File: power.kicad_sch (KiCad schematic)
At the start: 90 parts

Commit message: More work in progres
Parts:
- L41, L42, L43, L44, L45, L46, L47, L48: renamed from L?; value L_Ferrite_Power -> 100
- R402: renamed from R?; value 30k -> 51k
- R403: renamed from R?; value 240k -> 180k
- R432: renamed from R?; value 20k -> 12k
- R433: renamed from R?; value 160k -> 240k
- gave numbers to parts that had none: 76
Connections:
- net +1V8A: now also U42.11 (OUT2), U42.12 (OUT2); no longer U42.14 (OUT1), U42.15 (OUT1)
- net +2V5: now also U42.14 (OUT1), U42.15 (OUT1); no longer U41.14 (OUT1), U41.15 (OUT1)
- net +3V3A: now also U41.11 (OUT2), U41.12 (OUT2); no longer U42.11 (OUT2), U42.12 (OUT2)
- net +5VA: now also U41.14 (OUT1), U41.15 (OUT1); no longer U41.11 (OUT2), U41.12 (OUT2)
- net at C433.2, R431.1, R432.2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: now also U42.10 (FB2); no longer U42.16 (FB1)
- net at C414.2, R411.1, R412.2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: now also U41.10 (FB2); no longer U42.10 (FB2)
- net at U42.4 (IN2), U42.5 (IN2), U42.6 (EN2): now also C431.1, L44.2; no longer C411.1, C412.1, L42.2
- net at U42.7 (NR_SS2): now also C432.1; no longer C413.1
- net at C404.2, R401.1, R402.2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: now also U41.16 (FB1); no longer U41.10 (FB2)
- net at U42.1 (IN1), U42.2 (IN1), U42.20 (EN1): now also C421.1, L43.2; no longer C431.1, L44.2
- net at C401.1, C402.1, L41.2: now also U41.1 (IN1), U41.2 (IN1), U41.20 (EN1); no longer U41.4 (IN2), U41.5 (IN2), U41.6 (EN2)
- net at C403.1: now also U41.19 (NR_SS1); no longer U41.7 (NR_SS2)
- net at C423.2, R421.1, R422.2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: now also U42.16 (FB1); no longer U41.16 (FB1)
- net at C422.1: now also U42.19 (NR_SS1); no longer U41.19 (NR_SS1)
- new net: C411.1, C412.1, L42.2, U41.4 (IN2), U41.5 (IN2), U41.6 (EN2)
- new net: C413.1, U41.7 (NR_SS2)
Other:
- note added: "Margined to 5.1V"
- moved on the sheet: L47, R461, TP462

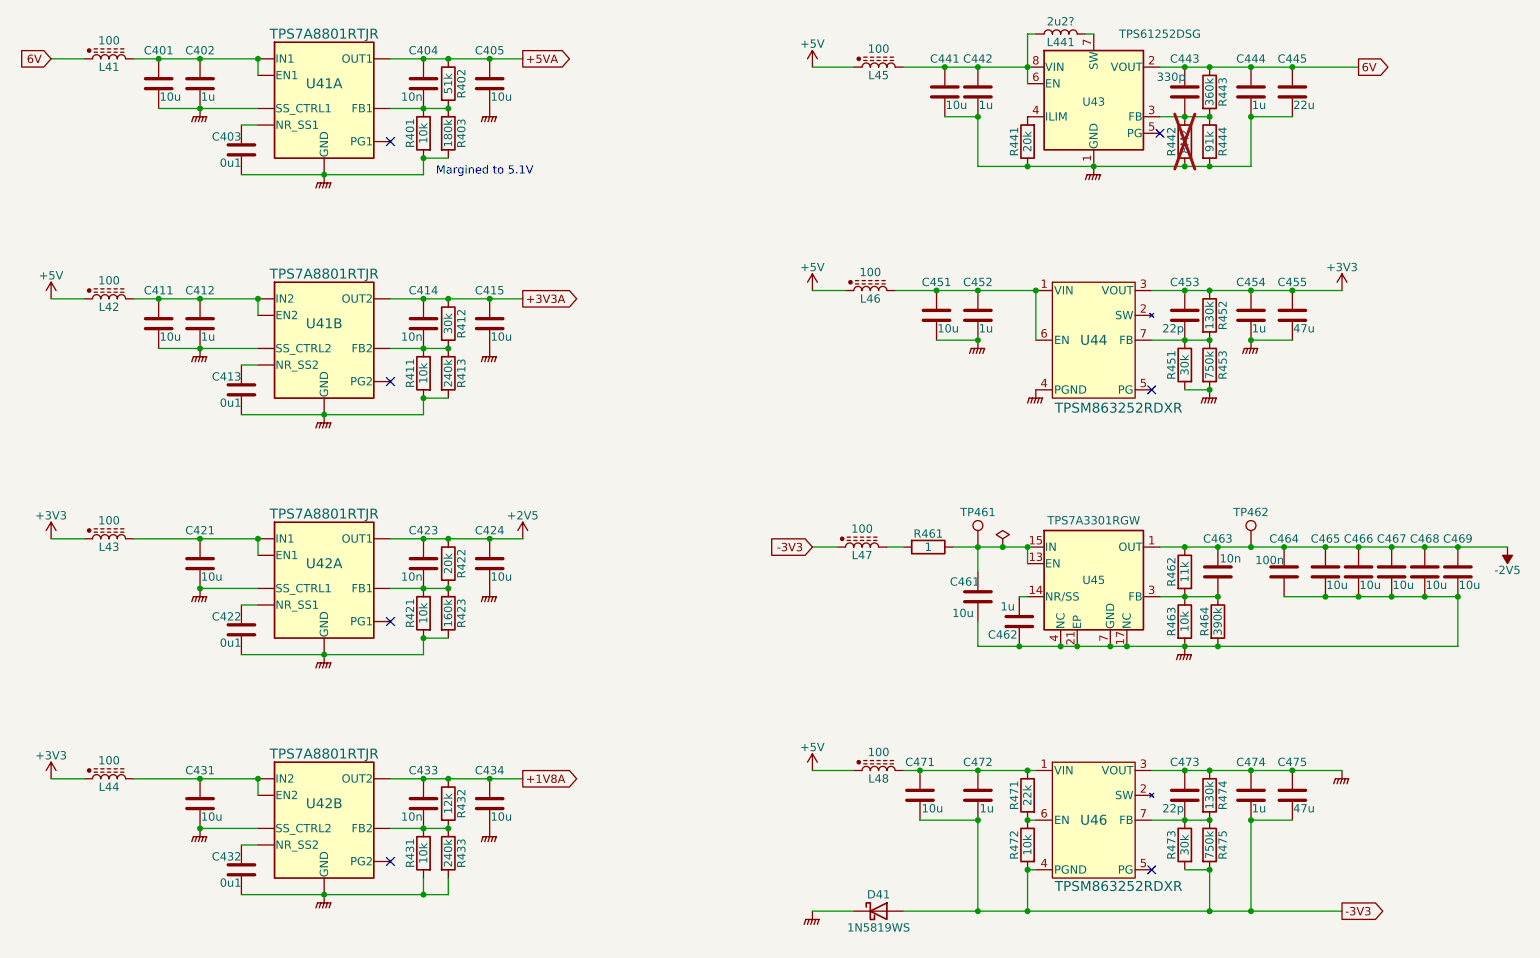
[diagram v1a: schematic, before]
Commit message: Analog side is more or less complete.
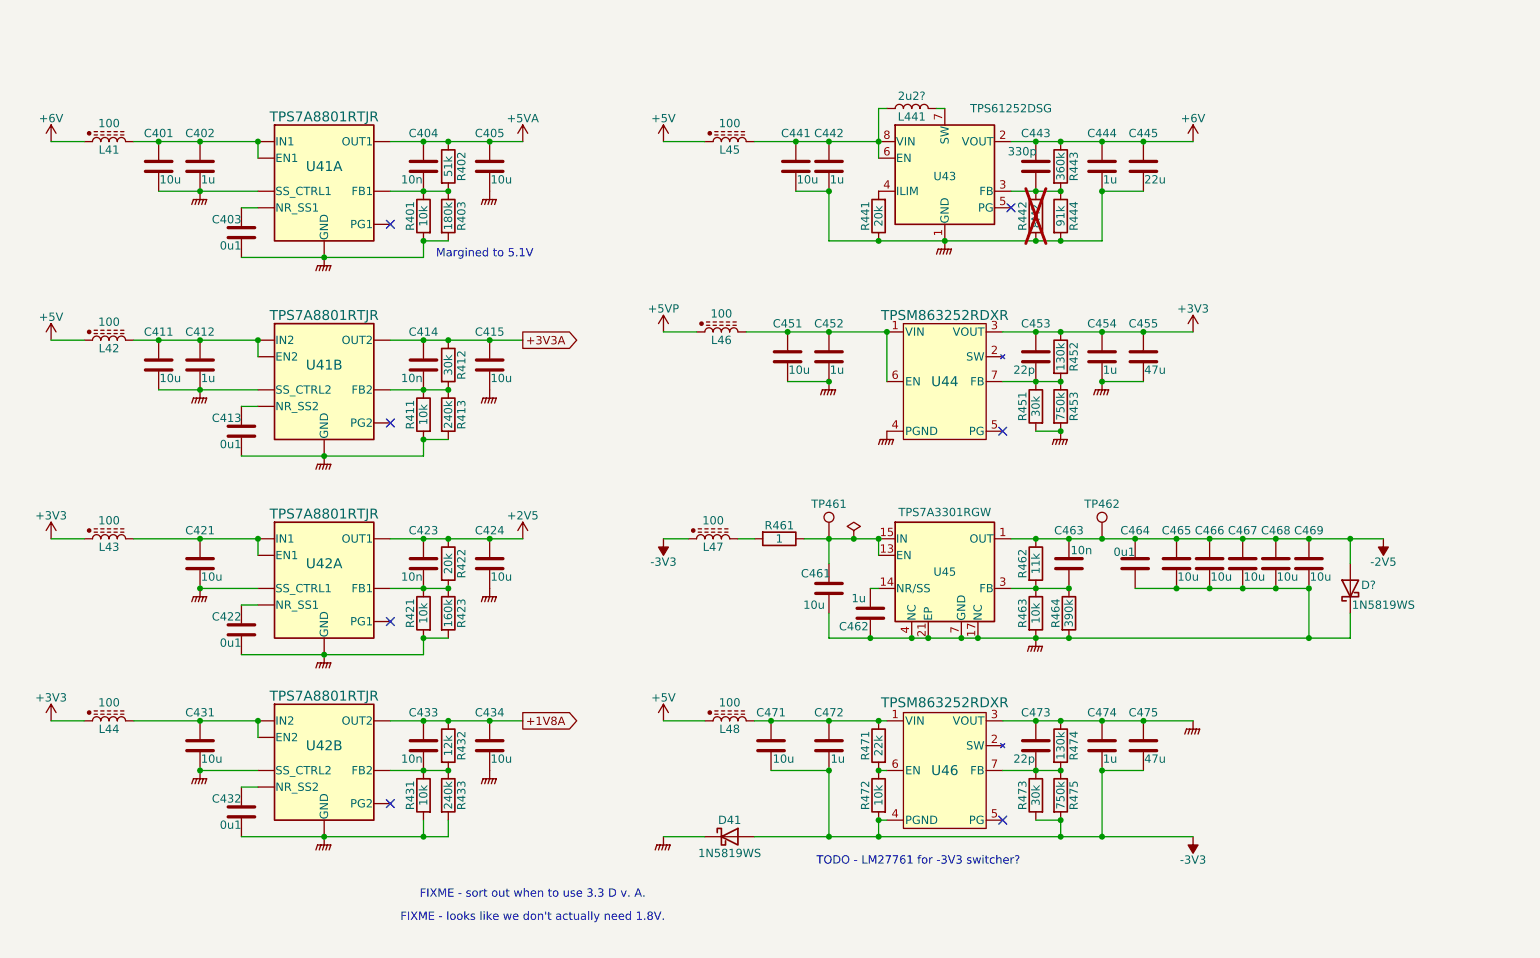
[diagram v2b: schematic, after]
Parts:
- added D?: 1N5819WS, Diode_SMD:D_SOD-323, symbol Diode:1N5819WS
- C464: value 100n -> 0u1
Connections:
- net +5V: no longer L46.1
- net -2V5: now also D?.2 (A)
- net GND: now also D?.1 (K)
- net 6V renamed +6V
- new net +5VP: L46.1
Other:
- note added: "FIXME - looks like we don't actually need 1.8V."
- note added: "FIXME - sort out when to use 3.3 D v. A."
- note added: "TODO - LM27761 for -3V3 switcher?"
- moved on the sheet: C401, C402, C403, C404, C405, C411, C412, C413, C414, C415, C431, C432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

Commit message: Little simplifications etc.
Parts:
- added TP41, TP42, TP43, TP44, TP45, TP46, TP47, TP48: TestPoint, Parts:TestPoint_THTPad_D1.0mm_Drill0.5mm, symbol Connector:TestPoint
- gave numbers to parts that had none: 1
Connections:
- net +1V8A: now also TP47.1
- net +2V5: now also TP45.1
- net +3V3: now also TP43.1
- net +3V3A: now also TP44.1
- net +5VA: now also TP41.1
- net +6V: now also TP42.1
- net -2V5: now also TP46.1
- net -3V3: now also TP48.1

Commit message: Schematic complete, maybe
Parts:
- removed C467, C468, C469: 10u, Capacitor_SMD:C_0402_1005Metric, symbol Device:C
- removed TP461, TP462: TestPoint, Parts:TestPoint_THTPad_D1.0mm_Drill0.5mm, symbol Connector:TestPoint
- added C422, C432: 1u, Capacitor_SMD:C_0402_1005Metric, symbol Device:C
- added C456, C476: 22u, Capacitor_SMD:C_0805_2012Metric, symbol Device:C
- added TP49: TestPoint, Parts:TestPoint_THTPad_D1.0mm_Drill0.5mm, symbol Connector:TestPoint
- C404, C414, C423, C433: footprint (none) -> Capacitor_SMD:C_0603_1608Metric; LCSC (none) -> C307500
- C405, C415, C424, C434: footprint Capacitor_SMD:C_0402_1005Metric -> Capacitor_SMD:C_0603_1608Metric; LCSC C15525 -> C96446
- C443: footprint Capacitor_SMD:C_0402_1005Metric -> Capacitor_SMD:C_0603_1608Metric; LCSC C52923 -> C1664
- C453, C473: footprint (none) -> Capacitor_SMD:C_0402_1005Metric; LCSC (none) -> C1555
- C455, C475: value 47u -> 22u; LCSC C16780 -> C45783
- C461: footprint Capacitor_SMD:C_0402_1005Metric -> Capacitor_SMD:C_0603_1608Metric; JLCPCB C440198 -> (none); LCSC (none) -> C96446; Voltage 50V -> (none)
- C462: JLCPCB C52923 -> (none); LCSC (none) -> C52923
- C463: footprint Capacitor_SMD:C_0402_1005Metric -> Capacitor_SMD:C_0603_1608Metric; JLCPCB C15195 -> (none); LCSC (none) -> C307500
- C464: JLCPCB C307331 -> (none); LCSC (none) -> C307331
- C465, C466: value 10u -> 22u; footprint Capacitor_SMD:C_0402_1005Metric -> Capacitor_SMD:C_0805_2012Metric; LCSC C15525 -> C45783
- L41, L42, L43, L44, L45, L47, L48: value 100 -> 600; footprint (none) -> Inductor_SMD:L_0603_1608Metric; LCSC (none) -> C1002
- L46: footprint (none) -> Inductor_SMD:L_0603_1608Metric; LCSC (none) -> C14709
- R432: value 12k -> 51k
- R433: value 240k -> 56k
- R442: value 8M2 -> 2M; now fitted
- R461: JLCPCB C25334 -> (none)
- R462: JLCPCB C22795 -> (none)
- R463: JLCPCB C25744 -> (none)
- U41, U42, U43: now left out of the parts list
- U44, U46: LCSC (none) -> C19632640
- U45: JLCPCB C90082 -> (none); LCSC (none) -> C90082; now left out of the parts list
- renumbered C422 to C425, C432 to C435
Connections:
- net +3V3: now also C456.1
- net -3V3: now also C476.2
- net GND: now also C422.2, C432.2, C456.2, C476.1
- net at C431.1, L44.2, U42.4 (IN2)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: now also C432.1
- net at C421.1, L43.2, U42.1 (IN1)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: now also C422.1
- net at C461.1, R461.1, U45.13 (EN)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: now also TP49.1
- net +1V8A renamed +5V6A
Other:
- note added: "Margined to 6.15V"
- note removed: "FIXME - looks like we don't actually need 1.8V."
- note removed: "FIXME - sort out when to use 3.3 D v. A."
- moved on the sheet: C401, C402, C411, C412, C421, C431, C441, C442, C443, C444, C445, C451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

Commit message: Part selection
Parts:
- C443: value 330p -> 220p
- C462: Voltage 25V -> (none)
- D41, D42: symbol Diode:1N5819WS -> Parts:1N5819WS; LCSC (none) -> C191023
- L441: value 2u2? -> 1u5; footprint (none) -> Inductor_SMD:L_1008_2520Metric; now left out of the parts list
- R401, R411, R421, R431, R472: footprint (none) -> Resistor_SMD:R_0402_1005Metric; LCSC (none) -> C25744
- R402, R432: footprint (none) -> Resistor_SMD:R_0402_1005Metric; LCSC (none) -> C25794
- R403: footprint (none) -> Resistor_SMD:R_0603_1608Metric; LCSC (none) -> C22827
- R412, R451: footprint (none) -> Resistor_SMD:R_0603_1608Metric; LCSC (none) -> C22984
- R413: footprint (none) -> Resistor_SMD:R_0603_1608Metric; LCSC (none) -> C4197
- R422: footprint (none) -> Resistor_SMD:R_0402_1005Metric; LCSC (none) -> C25765
- R423: footprint (none) -> Resistor_SMD:R_0603_1608Metric; LCSC (none) -> C22813
- R433: footprint (none) -> Resistor_SMD:R_0402_1005Metric; LCSC (none) -> C25796
- R441: value 20k -> 6k8; footprint (none) -> Resistor_SMD:R_0603_1608Metric; LCSC (none) -> C23212
- R442: footprint (none) -> Resistor_SMD:R_0603_1608Metric; LCSC (none) -> C22976
- R443: footprint (none) -> Resistor_SMD:R_0603_1608Metric; LCSC (none) -> C23146
- R444: footprint (none) -> Resistor_SMD:R_0603_1608Metric; LCSC (none) -> C23265
- R452: footprint (none) -> Resistor_SMD:R_0603_1608Metric; LCSC (none) -> C22795
- R453: footprint (none) -> Resistor_SMD:R_0603_1608Metric; LCSC (none) -> C23240
- R461: footprint Resistor_SMD:R_1206_3216Metric -> Resistor_SMD:R_0603_1608Metric; LCSC (none) -> C22936
- R462: LCSC (none) -> C25950
- R463: LCSC (none) -> C25744
- R464: LCSC (none) -> C23150
- R471: footprint (none) -> Resistor_SMD:R_0402_1005Metric; LCSC (none) -> C25768
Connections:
- net +2V5: now also U42.11 (OUT2), U42.12 (OUT2); no longer U42.14 (OUT1), U42.15 (OUT1)
- net +3V3: no longer L44.1
- net +3V3A: now also U42.14 (OUT1), U42.15 (OUT1); no longer U41.11 (OUT2), U41.12 (OUT2)
- net +5V6A: now also U41.11 (OUT2), U41.12 (OUT2); no longer U42.11 (OUT2), U42.12 (OUT2)
- net +6V: now also L44.1
- net at C433.2, R431.1, R432.2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: now also U41.10 (FB2); no longer U42.10 (FB2)
- net at U42.4 (IN2), U42.5 (IN2), U42.6 (EN2): now also C421.1, C422.1, L43.2; no longer C431.1, C432.1, L44.2
- net at U42.7 (NR_SS2): now also C425.1; no longer C435.1
- net at C414.2, R411.1, R412.2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: now also U42.16 (FB1); no longer U41.10 (FB2)
- net at U41.4 (IN2), U41.5 (IN2), U41.6 (EN2): now also C431.1, C432.1, L44.2; no longer C411.1, C412.1, L42.2
- net at C413.1: now also U42.19 (NR_SS1); no longer U41.7 (NR_SS2)
- net at C423.2, R421.1, R422.2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: now also U42.10 (FB2); no longer U42.16 (FB1)
- net at U42.1 (IN1), U42.2 (IN1), U42.20 (EN1): now also C411.1, C412.1, L42.2; no longer C421.1, C422.1, L43.2
- new net: C435.1, U41.7 (NR_SS2)
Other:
- moved on the sheet: U41B, U42A, U42B

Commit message: ERC passes.
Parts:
- added C406, C416, C426, C436: 10u, Capacitor_SMD:C_0603_1608Metric, symbol Device:C
- C405, C415, C424, C434: value 10u -> 1u; footprint Capacitor_SMD:C_0603_1608Metric -> Capacitor_SMD:C_0402_1005Metric; LCSC C96446 -> C52923
- TP41, TP42, TP43, TP44, TP45, TP46, TP47, TP48, TP49: footprint Parts:TestPoint_THTPad_D1.0mm_Drill0.5mm -> Parts:TestPoint; now left out of the parts list
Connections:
- net +2V5: now also C426.1
- net +3V3A: now also C416.1
- net +5V6A: now also C436.1
- net +5VA: now also C406.1
- net GND renamed GNDPWR
- net GNDPWR: now also C406.2, C416.2, C426.2, C436.2
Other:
- moved on the sheet: C405, C415, C424, C434, C441, C461, C471, C472, L45, L46, L47, L48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

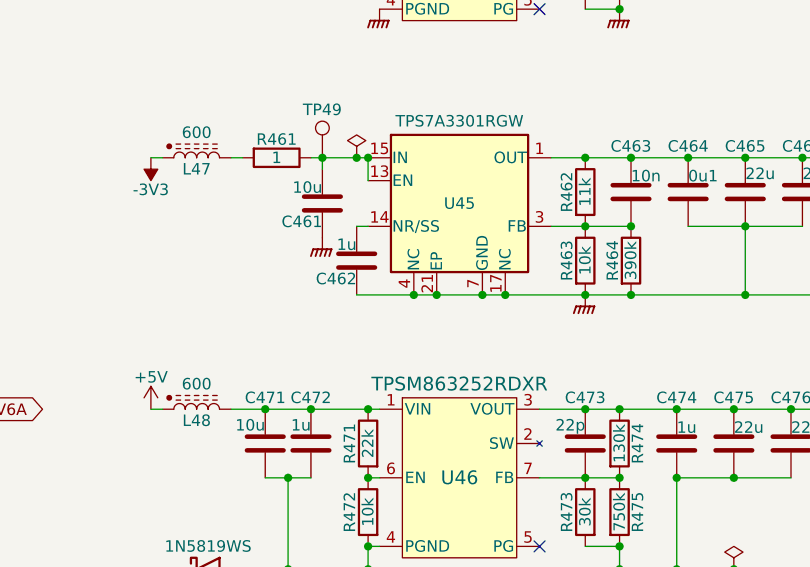
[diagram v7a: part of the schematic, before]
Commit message: Layout underway
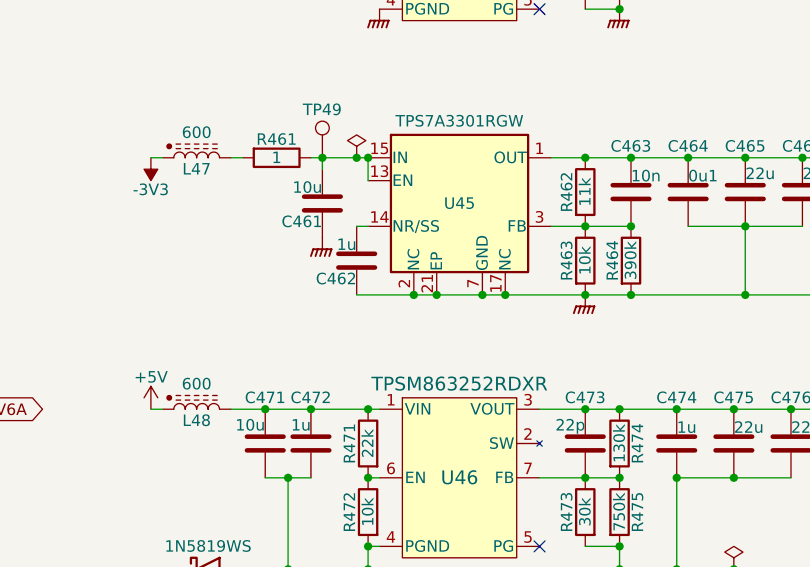
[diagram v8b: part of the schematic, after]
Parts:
- U45: footprint Package_DFN_QFN:Texas_RGW0020A_VQFN-20-1EP_5x5mm_P0.65mm_EP3.15x3.15mm_ThermalVias -> Package_DFN_QFN:Texas_RGW0020A_VQFN-20-1EP_5x5mm_P0.65mm_EP3.15x3.15mm
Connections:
- net GNDPWR: now also U45.2 (NC)
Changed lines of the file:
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@@
 			)
 		)
-		(property "Footprint" "Package_DFN_QFN:Texas_RGW0020A_VQFN-20-1EP_5x5mm_P0.65mm_EP3.15x3.15mm_ThermalVias"
+		(property "Footprint" "Package_DFN_QFN:Texas_RGW0020A_VQFN-20-1EP_5x5mm_P0.65mm_EP3.15x3.15mm"
 			(at 177.8 96.52 0)
 			(effects
@@
 		(pin "9"
 		)
+		(pin "2"
+		)
 		(instances
